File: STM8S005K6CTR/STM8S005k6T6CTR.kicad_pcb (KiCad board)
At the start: 2 copper layers, 7 parts, among them IC2 LM2671M-5.0_NOPB, J1 282837-2

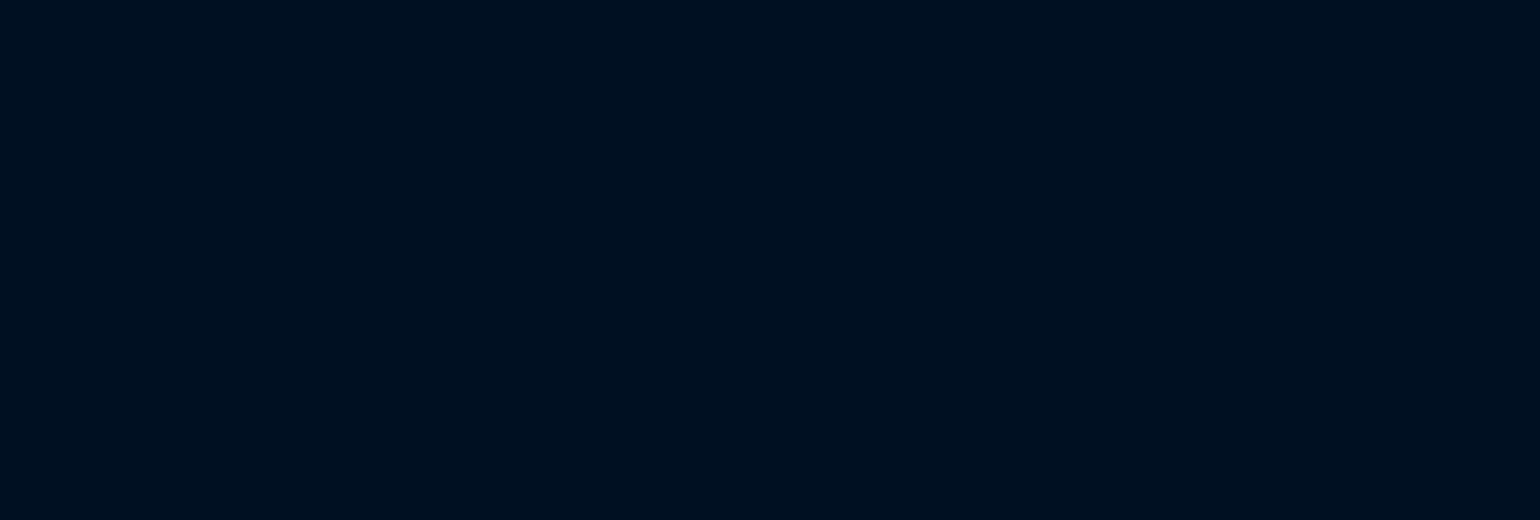
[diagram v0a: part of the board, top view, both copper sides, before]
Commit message: [STM8S005K6T6CTR] Calculations: calculated crystal components. Board scheme: Added crystal to scheme (with footprint). Added part of output pins.
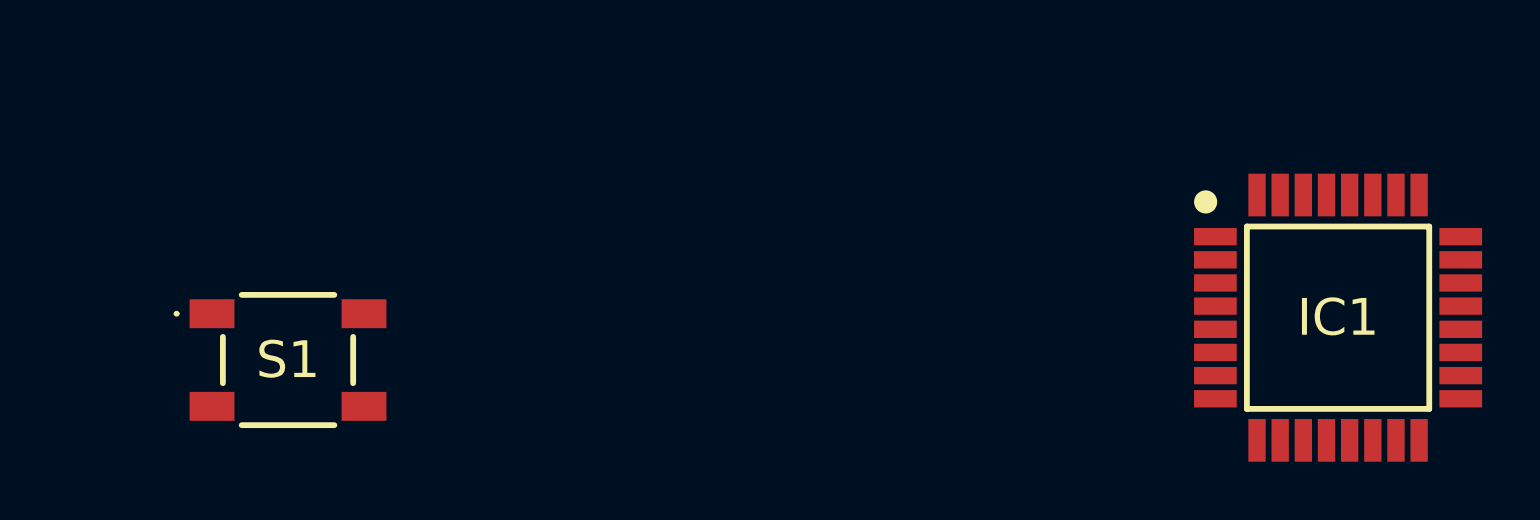
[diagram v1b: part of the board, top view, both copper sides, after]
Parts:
- added IC1: STM8S005K6T6CTR, STM8S005K6CTR:QFP80P900X900X160-32N, F.Cu at (164.5, 102.0)
- added S1: PTS647SK70SMTR2N_LFS, PTS647SK70SMTR2N LFS:PTS647SK70SMTR2NLFS, F.Cu at (128.2, 103.5)
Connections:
- C6 pad 1: GND -> +5V
- IC2 pad 4: GND -> +5V
- L1 pad 2: GND -> +5V

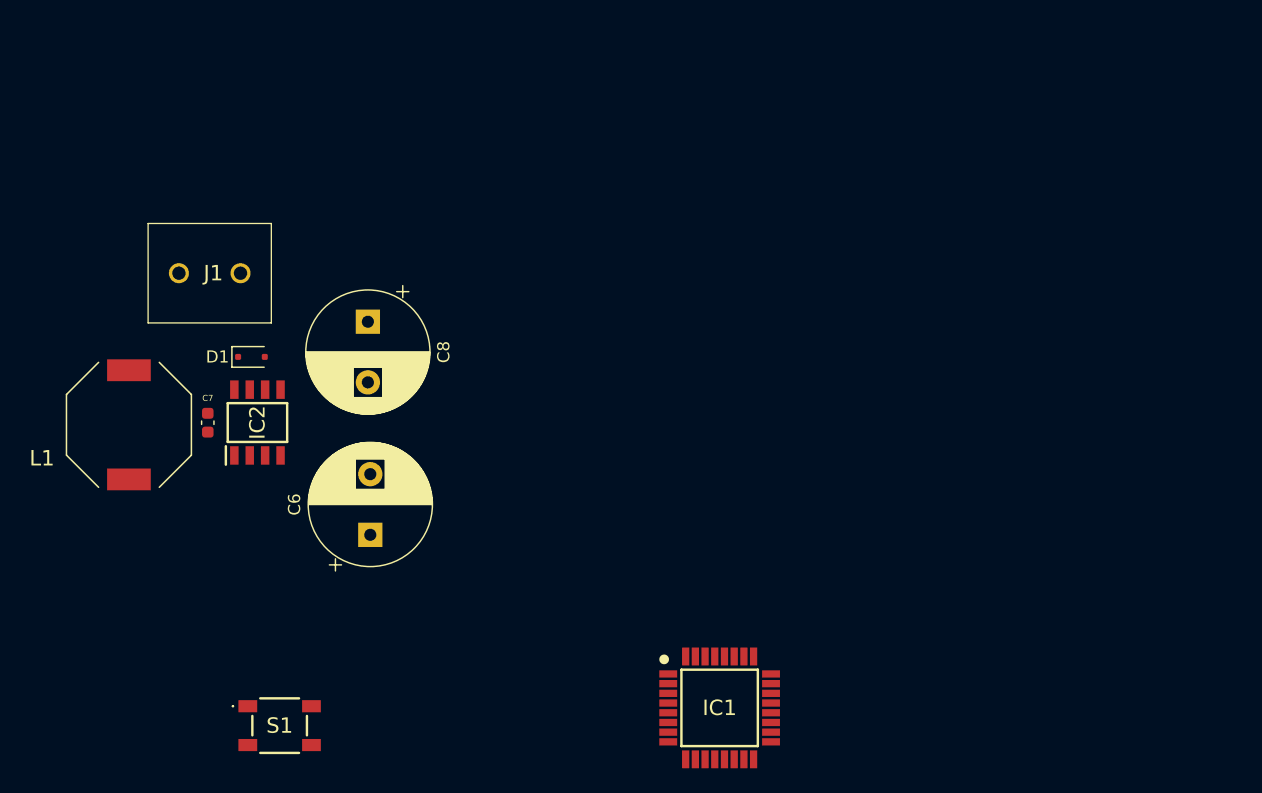
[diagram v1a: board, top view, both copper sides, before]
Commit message: [STM8S005K6T6CTR] Board scheme: Footprints layout. Crystal routing.
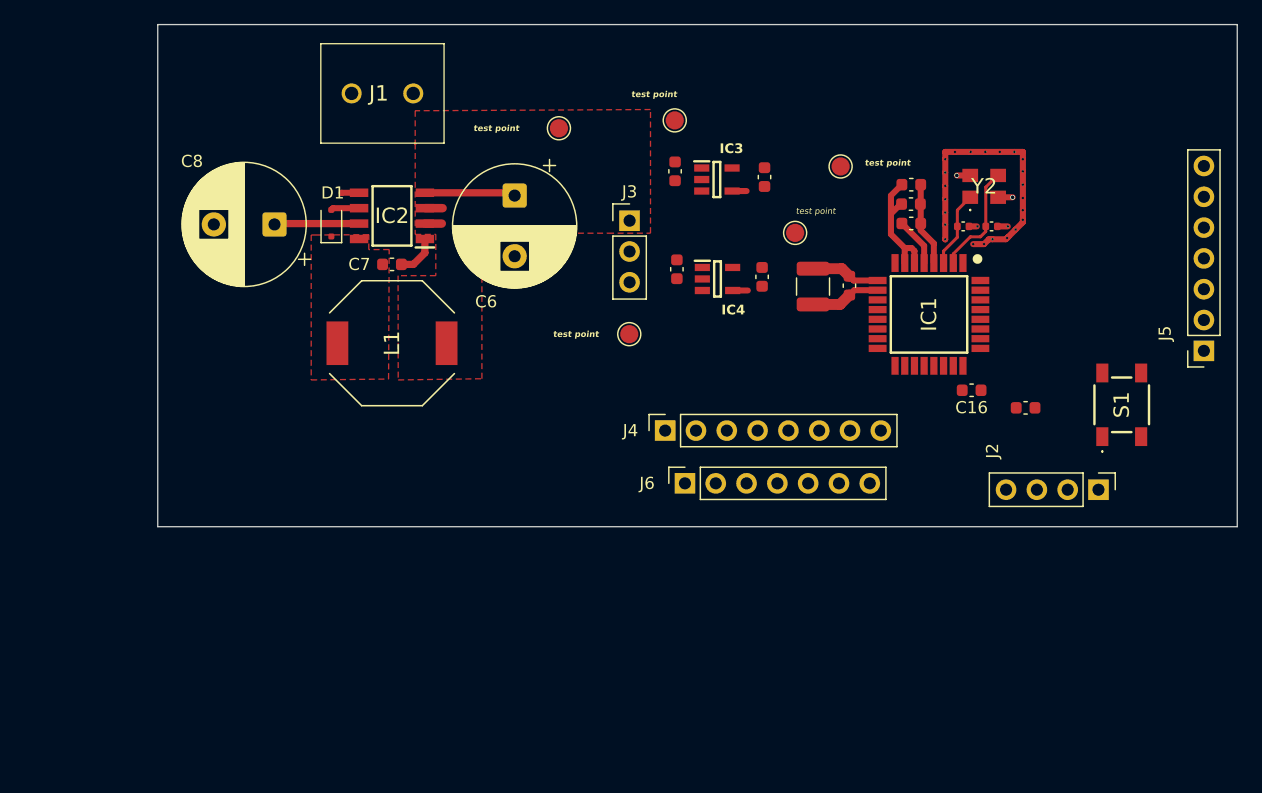
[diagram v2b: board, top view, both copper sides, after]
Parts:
- added C1: 1u, Capacitor_SMD:C_0603_1608Metric, F.Cu at (180.3, 62.1)
- added C10: 6p, Capacitor_SMD:C_0402_1005Metric, F.Cu at (186.9, 62.3)
- added C11: 6p, Capacitor_SMD:C_0402_1005Metric, F.Cu at (184.6, 62.3)
- added C12: 100n, Capacitor_SMD:C_0603_1608Metric, F.Cu at (175.2, 67.2)
- added C13: 1u, Capacitor_SMD:C_1210_3225Metric, F.Cu at (172.2, 67.3)
- added C14: 1u, Capacitor_SMD:C_0603_1608Metric, F.Cu at (160.8, 57.8)
- added C15: 1u, Capacitor_SMD:C_0603_1608Metric, F.Cu at (168.0, 66.5)
- added C16: 100n, Capacitor_SMD:C_0603_1608Metric, F.Cu at (185.3, 75.8)
- added C2: 100n, Capacitor_SMD:C_0603_1608Metric, F.Cu at (180.3, 60.5)
- added C3: 100n, Capacitor_SMD:C_0603_1608Metric, F.Cu at (180.3, 58.9)
- added C4: 1u, Capacitor_SMD:C_0603_1608Metric, F.Cu at (161.0, 65.9)
- added C5: 1u, Capacitor_SMD:C_0603_1608Metric, F.Cu at (168.2, 58.3)
- added C9: 100n, Capacitor_SMD:C_0603_1608Metric, F.Cu at (189.7, 77.3)
- added IC3: ADPL40502AUJZ-3.3-R7, ADPL40502AUJZ-3.3-R7:SOT95P280X100-5N, F.Cu at (164.3, 58.5)
- added IC4: ADPL40502AUJZ-3.3-R7, ADPL40502AUJZ-3.3-R7:SOT95P280X100-5N, F.Cu at (164.3, 66.7)
- added J2: Conn_01x04_Pin, Connector_PinHeader_2.54mm:PinHeader_1x04_P2.54mm_Vertical, F.Cu at (195.7, 84.0)
- added J3: Conn_01x03_Pin, Connector_PinHeader_2.54mm:PinHeader_1x03_P2.54mm_Vertical, F.Cu at (157.1, 61.9)
- added J4: Conn_01x08_Pin, Connector_PinSocket_2.54mm:PinSocket_1x08_P2.54mm_Vertical, F.Cu at (160.0, 79.2)
- added J5: Conn_01x07_Pin, Connector_PinSocket_2.54mm:PinSocket_1x07_P2.54mm_Vertical, F.Cu at (204.4, 72.6)
- added J6: Conn_01x07_Pin, Connector_PinSocket_2.54mm:PinSocket_1x07_P2.54mm_Vertical, F.Cu at (161.6, 83.5)
- added TP2: TestPoint, TestPoint:TestPoint_Pad_D1.5mm, F.Cu at (151.2, 54.2)
- added TP3: TestPoint, TestPoint:TestPoint_Pad_D1.5mm, F.Cu at (157.1, 71.2)
- added TP4: TestPoint, TestPoint:TestPoint_Pad_D1.5mm, F.Cu at (160.8, 53.6)
- added TP5: TestPoint, TestPoint:TestPoint_Pad_D1.5mm, F.Cu at (174.5, 57.4)
- added TP6: TestPoint, TestPoint:TestPoint_Pad_D1.5mm, F.Cu at (170.7, 62.9)
- added Y2: 8 Mhz, ECS-80-33820-CVY-TR3:ECS80833B2QCVYTR3, F.Cu at (186.3, 59.0)
- moved S1 74.3 mm to (197.7, 77.0), turned to 90 degrees
- moved IC1 36.7 mm to (181.8, 69.6), turned to -90 degrees
- moved C6 30.4 mm to (147.6, 59.8), turned to -90 degrees
- moved L1 22.7 mm to (137.5, 72.0), turned to 90 degrees
- moved IC2 20.3 mm to (137.5, 61.5), turned to 180 degrees
- moved C7 20.0 mm to (137.5, 65.5), turned to 0 degrees
- moved J1 17.4 mm to (134.2, 51.4), turned to 0 degrees
- moved D1 12.8 mm to (132.5, 62.1), turned to 90 degrees
- moved C8 11.1 mm to (127.8, 62.2), turned to 180 degrees
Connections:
- net +5V renamed +5V (External)
- IC1 pad 11: unconnected-(IC1-[I2C_SDA]AIN5/PB5-Pad11) -> 11
- IC1 pad 12: unconnected-(IC1-[I2C_SCL]_AIN4/PB4-Pad12) -> 12
- IC1 pad 13: unconnected-(IC1-[TIM1_ETR]_AIN3/PB3-Pad13) -> 13
- IC1 pad 14: unconnected-(IC1-[TIM1_CH3N]_AIN2/PB2-Pad14) -> 14
- IC1 pad 15: unconnected-(IC1-[TIM1_CH2N]_AIN1/PB1-Pad15) -> 15
- IC1 pad 16: unconnected-(IC1-[TIM1_CH1N]_AIN0/PB0-Pad16) -> 16
- IC1 pad 17: unconnected-(IC1-PE5/SPI_NSS-Pad17) -> 17
- IC1 pad 18: unconnected-(IC1-PC1_(HS)/TIM1_CH1/UART2_CLK-Pad18) -> 18
- IC1 pad 19: unconnected-(IC1-PC2_(HS)/TIM1_CH2-Pad19) -> 19
- IC1 pad 2: unconnected-(IC1-OSCIN/PA1-Pad2) -> Net-(IC1-OSCIN/PA1)
- IC1 pad 20: unconnected-(IC1-PC3_(HS)/TIM1_CH3-Pad20) -> 20
- IC1 pad 21: unconnected-(IC1-PC4_(HS)/TIM1_CH4-Pad21) -> 21
- IC1 pad 22: unconnected-(IC1-PC5_(HS)/SPI_SCK-Pad22) -> 22
- IC1 pad 23: unconnected-(IC1-PC6_(HS)/SPI_MOSI-Pad23) -> 23
- IC1 pad 24: unconnected-(IC1-PC7_(HS)/SPI_MISO-Pad24) -> Net-(IC1-PC7_(HS)/SPI_MISO)
- IC1 pad 25: unconnected-(IC1-PD0_(HS)/_TIM3_CH2_[TIM1_BKIN]_[CLK_CCO]-Pad25) -> 25
- IC1 pad 27: unconnected-(IC1-PD2_(HS)/TIM3_CH1_[TIM2_CH3]-Pad27) -> 27
- IC1 pad 28: unconnected-(IC1-PD3_(HS)/TIM2_CH2_[ADC_ETR]-Pad28) -> 28
- IC1 pad 29: unconnected-(IC1-PD4_(HS)/TIM2_CH1_[BEEP]-Pad29) -> 29
- IC1 pad 3: unconnected-(IC1-OSCOUT/PA2-Pad3) -> Net-(IC1-OSCOUT/PA2)
- IC1 pad 30: unconnected-(IC1-PD5_/UART2_TX-Pad30) -> 30
- IC1 pad 31: unconnected-(IC1-PD6_/UART2_RX-Pad31) -> 31
- IC1 pad 32: unconnected-(IC1-PD7/TLI_[TIM1_CH4]-Pad32) -> 32
- IC1 pad 6: GND -> VDD
- IC1 pad 7: GND -> VDD
- IC1 pad 8: unconnected-(IC1-AIN12/PF4-Pad8) -> 8
- IC1 pad 9: GND -> VDDA
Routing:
- net NRST: track 0.00 -> 24.3 mm, vias 0 -> 23
- net GND: track 0.00 -> 18.9 mm, vias 0 -> 4
- net VDD: track 0.00 -> 10.6 mm
- net Net-(IC1-OSCIN/PA1): track 0.00 -> 9.27 mm
- net +5V (External): track 0.00 -> 7.50 mm
- net +24V: track 0.00 -> 7.00 mm
- net Net-(IC1-OSCOUT/PA2): track 0.00 -> 6.67 mm
- net VDDA: track 0.00 -> 5.73 mm
- net Net-(IC1-VCAP): track 0.00 -> 4.02 mm
- net Net-(IC2-CB): track 0.00 -> 3.48 mm
- net unconnected-(IC2-SYNC-Pad3): track 0.00 -> 1.46 mm
- net unconnected-(IC2-ON/~{OFF}-Pad5): track 0.00 -> 1.45 mm
- net unconnected-(IC2-SS-Pad2): track 0.00 -> 1.39 mm
- net unconnected-(IC4-NC-Pad4): track 0.00 -> 1.25 mm
- net unconnected-(IC3-NC-Pad4): track 0.00 -> 1.20 mm
- added copper zone on F.Cu, net +5V (External)
- added copper zone on F.Cu, net Net-(D1-K)
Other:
- board outline added: 89 x 41.4 mm
